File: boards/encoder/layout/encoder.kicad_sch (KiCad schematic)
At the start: 6 parts, among them IC1 AS5047U-HTSM, J1 EncoderTab

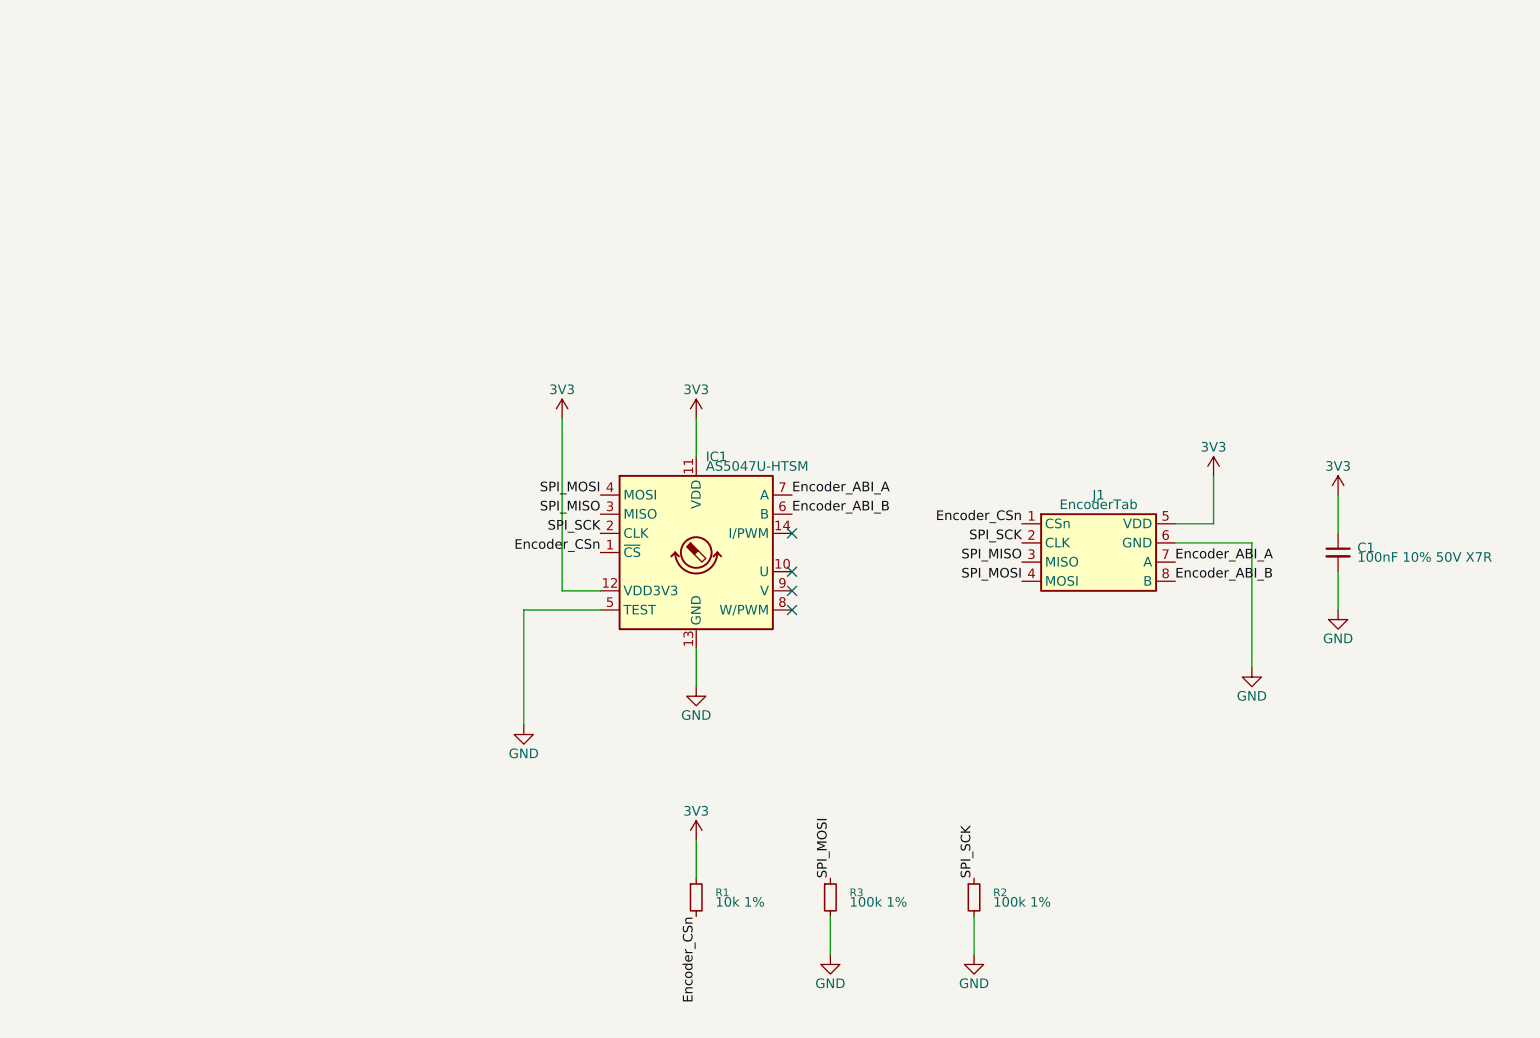
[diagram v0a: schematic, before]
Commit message: ✨ Place the schematics from per-sheet placement files
micras-pcb sch redraws each sheet pcb apply writes from
boards/<board>/schematic/<sheet>.toml: parts, wires, labels, power
symbols, titled frames, paper and title block, the root's sheet
symbols, and a ports column for the module sheets' extra labels. It
fails unless KiCad's netlist of the placed schematic equals pcb's.
make gen runs it after pcb apply; make check's sch gate fails on a part
without a placement, and tests/test_placement.py on any overlap.

The encoder and Bluetooth sheets are placed; the main board's DRIVERS
sheet is drafted.
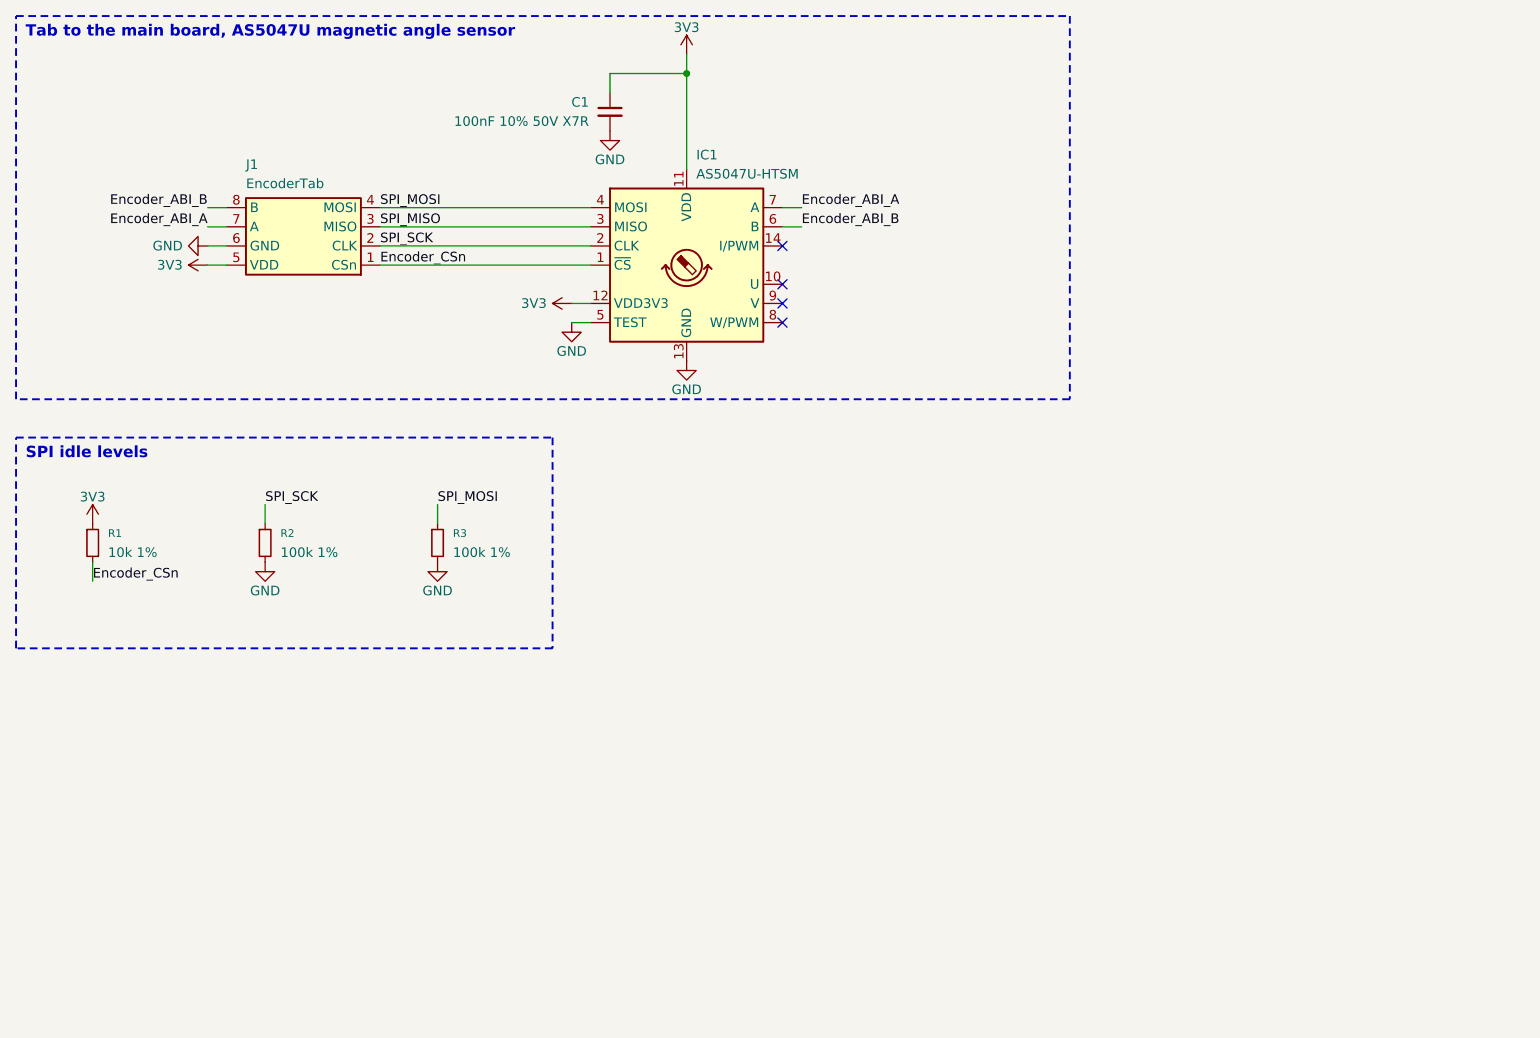
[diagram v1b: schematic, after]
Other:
- note added: "SPI idle levels"
- note added: "Tab to the main board, AS5047U magnetic angle sensor"
- title: (none) -> Wheel encoder
- moved on the sheet: C1, IC1, J1, R1, R2, R3
